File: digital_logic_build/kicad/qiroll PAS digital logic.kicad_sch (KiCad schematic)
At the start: 47 parts, among them J2 led_sw1, J3 accessory, J4 mode_thr_batt, J5 3_pin, U1 4093B, U2 4027B, U3 4093B, U5 4093B, U6 14538B, U7 MCP1799_3V3

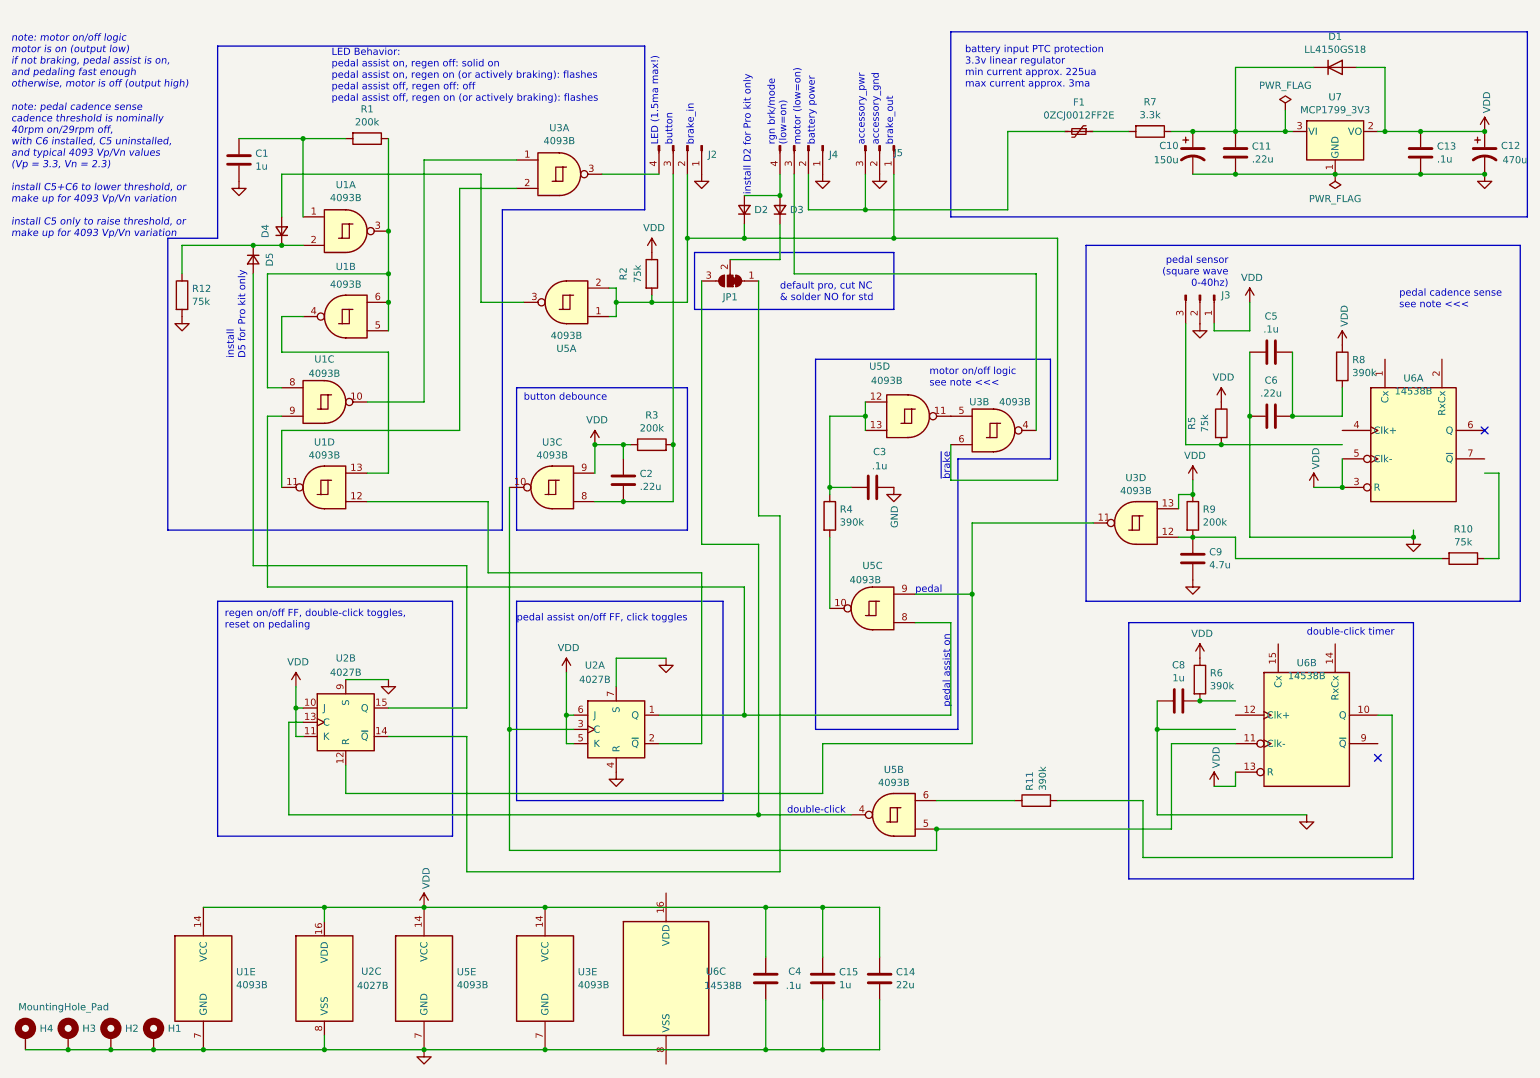
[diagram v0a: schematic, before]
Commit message: update pcb to new kicad
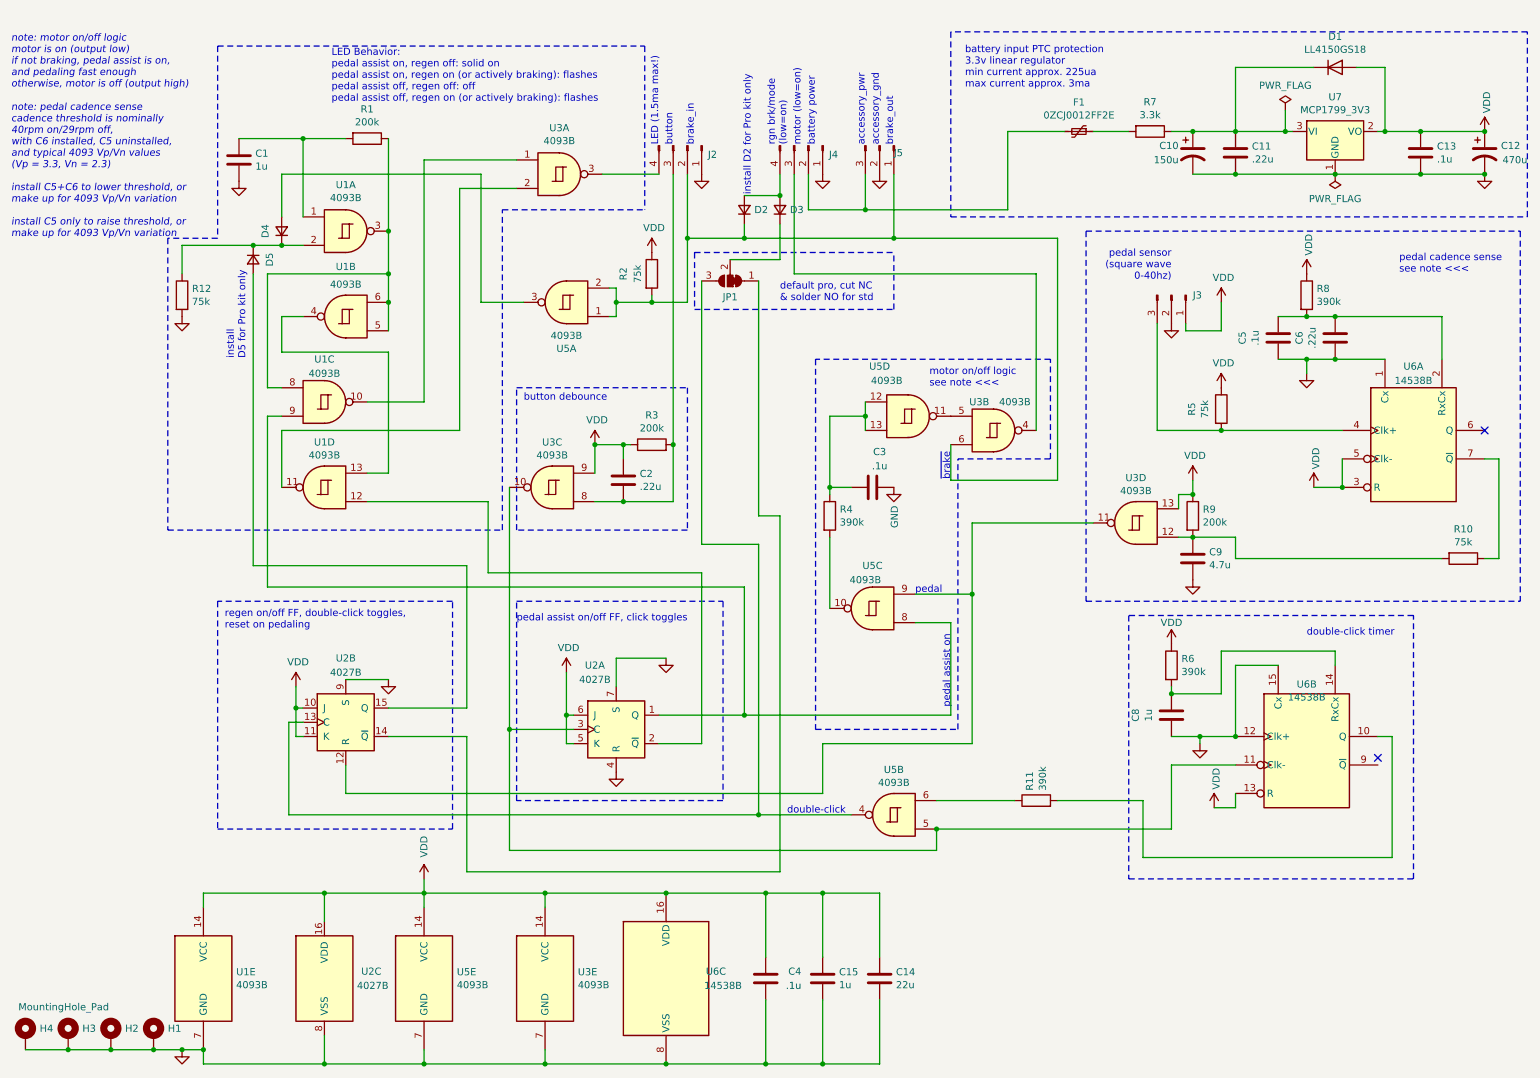
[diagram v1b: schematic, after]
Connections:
- net GND: now also U6.1 (Cx), U6.12 (Clk+), U6.15 (Cx), U6.8 (VSS)
- net VDD: now also U6.16 (VDD)
- net at U6.2 (RxCx): now also C5.1, C6.1, R8.2
- net at U6.4 (Clk+): now also J3.3 (Pin_3), R5.2
- net at U6.7 (~{Q}): now also R10.1
- net at U6.14 (RxCx): now also C8.1, R6.2
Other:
- moved on the sheet: C5, C6, C8, J3, R5, R6, R8, U6B
